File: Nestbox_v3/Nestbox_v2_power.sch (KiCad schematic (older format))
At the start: 27 parts, among them J201 BATT_CONN_01X02, Q201 Q_PMOS_DGS, U201 TPS62745, U202 LTC3534, U203 LP5907

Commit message: finished V3 pcb. ORDERED
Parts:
- removed JP201: VAA_Jumper_SELECT_Dual, Pin_Headers:Pin_Header_Straight_1x03, symbol Jumper_SELECT_Dual
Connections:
- net VAA: now also C204.1, U203.5 (VOUT)
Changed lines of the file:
@@
 L VAA #PWR013
 U 1 1 5B0757D1
-P 4700 5750
-F 0 "#PWR013" H 4700 5600 50  0001 C CNN
-F 1 "VAA" H 4717 5923 50  0000 C CNN
-F 2 "" H 4700 5750 50  0001 C CNN
-F 3 "" H 4700 5750 50  0001 C CNN
-	1    4700 5750
+P 4400 6050
+F 0 "#PWR013" H 4400 5900 50  0001 C CNN
+F 1 "VAA" H 4417 6223 50  0000 C CNN
+F 2 "" H 4400 6050 50  0001 C CNN
+F 3 "" H 4400 6050 50  0001 C CNN
+	1    4400 6050
 	1    0    0    -1
 $EndComp
@@
 	1950 6350 3100 6350
 Wire Wire Line
-	3100 6450 2900 6450
+	2900 6450 3100 6450
 Wire Wire Line
 	4100 6350 4400 6350
@@
 	2500 6850 2500 6750
 Wire Wire Line
-	2500 5550 2500 6450
+	2500 6350 2500 6450
 Connection ~ 2500 6350
 Wire Wire Line
@@
 	4400 6800 4400 6750
 $Comp
-L Jumper_SELECT_Dual JP201
-U 1 1 5B0C48C9
-P 4400 5800
-F 0 "JP201" H 4450 5700 50  0000 L CNN
-F 1 "VAA_Jumper_SELECT_Dual" H 4400 5900 50  0000 C BNN
-F 2 "Pin_Headers:Pin_Header_Straight_1x03" H 4400 5800 50  0001 C CNN
-F 3 "" H 4400 5800 50  0001 C CNN
-	1    4400 5800
-	0    -1   -1   0
-$EndComp
-Wire Wire Line
-	4700 5750 4700 5800
-Wire Wire Line
-	4700 5800 4500 5800
-Wire Wire Line
-	4400 5550 2500 5550
-$Comp
 L LTC3534 U202

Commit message: exchanged both inductor footprints.
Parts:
- L201: value 4.7uH -> 5uH; MFG_PN XFL3010-472MEB -> (none); MPN (none) -> MSS7341-502NLD
- L202: value 5uH -> 4.7uH; MFR_PN MSS7341-502NLD -> (none); MPN (none) -> XFL3010-472MEB
- Q201: value Q_PMOS_DGS -> TPH1R712MDL1Q; MPN (none) -> TPH1R712MDL1Q
- R201: value 100k -> 82k
- R202: value 50k -> 47k
- R204: value 162k -> 162k 1%
- R205: value 649k -> 649k 1%
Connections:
- net at C205.1, JP203.1, U201.5 (VOUT): now also L202.2; no longer L201.2
- net at L201.1: now also U202.5 (SW1); no longer U201.2 (SW)
- net at L202.1: now also U201.2 (SW); no longer U202.5 (SW1)
- net at U202.6 (SW2): now also L201.2; no longer L202.2
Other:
- moved on the sheet: L201, L202
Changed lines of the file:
@@
 L L L201
 U 1 1 5A021289
-P 4750 1500
-F 0 "L201" V 4940 1500 50  0000 C CNN
-F 1 "4.7uH" V 4849 1500 50  0000 C CNN
-F 2 "Inductors:Inductor_Taiyo-Yuden_NR-60xx_HandSoldering" H 4750 1500 50  0001 C CNN
-F 3 "" H 4750 1500 50  0001 C CNN
-F 4 "XFL3010-472MEB" V 4750 1500 60  0001 C CNN "MFG_PN"
-	1    4750 1500
+P 3700 3450
+F 0 "L201" V 3890 3450 50  0000 C CNN
+F 1 "5uH" V 3799 3450 50  0000 C CNN
+F 2 "Inductors:Inductor_Taiyo-Yuden_NR-60xx_HandSoldering" H 3700 3450 50  0001 C CNN
+F 3 "" H 3700 3450 50  0001 C CNN
+F 4 "MSS7341-502NLD" V 3700 3450 60  0001 C CNN "MPN"
+	1    3700 3450
 	0    -1   -1   0
 $EndComp
@@
 L L L202
 U 1 1 5A022A1C
-P 3700 3450
-F 0 "L202" V 3890 3450 50  0000 C CNN
-F 1 "5uH" V 3799 3450 50  0000 C CNN
-F 2 "Inductors:Inductor_Taiyo-Yuden_NR-30xx" H 3700 3450 50  0001 C CNN
-F 3 "" H 3700 3450 50  0001 C CNN
-F 4 "MSS7341-502NLD" V 3700 3450 60  0001 C CNN "MFR_PN"
-	1    3700 3450
+P 4750 1500
+F 0 "L202" V 4940 1500 50  0000 C CNN
+F 1 "4.7uH" V 4849 1500 50  0000 C CNN
+F 2 "Inductors:Inductor_Taiyo-Yuden_NR-30xx" H 4750 1500 50  0001 C CNN
+F 3 "" H 4750 1500 50  0001 C CNN
+F 4 "XFL3010-472MEB" V 4750 1500 60  0001 C CNN "MPN"
+	1    4750 1500
 	0    -1   -1   0
 $EndComp
@@
 P 5900 4300
 F 0 "R205" V 5693 4300 50  0000 C CNN
-F 1 "649k" V 5784 4300 50  0000 C CNN
+F 1 "649k 1%" V 5784 4300 50  0000 C CNN
 F 2 "Resistors_SMD:R_0603" V 5830 4300 50  0001 C CNN
 F 3 "" H 5900 4300 50  0001 C CNN
@@
 P 5650 4550
 F 0 "R204" H 5580 4504 50  0000 R CNN
-F 1 "162k" H 5580 4595 50  0000 R CNN
+F 1 "162k 1%" H 5580 4595 50  0000 R CNN
 F 2 "Resistors_SMD:R_0603" V 5580 4550 50  0001 C CNN
 F 3 "" H 5650 4550 50  0001 C CNN
@@
 P 2550 2350
 F 0 "R201" V 2343 2350 50  0000 C CNN
-F 1 "100k" V 2434 2350 50  0000 C CNN
+F 1 "82k" V 2434 2350 50  0000 C CNN
 F 2 "Resistors_SMD:R_0603" V 2480 2350 50  0001 C CNN
 F 3 "" H 2550 2350 50  0001 C CNN
@@
 P 2550 2800
 F 0 "R202" V 2343 2800 50  0000 C CNN
-F 1 "50k" V 2434 2800 50  0000 C CNN
+F 1 "47k" V 2434 2800 50  0000 C CNN
 F 2 "Resistors_SMD:R_0603" V 2480 2800 50  0001 C CNN
 F 3 "" H 2550 2800 50  0001 C CNN
@@
 P 9000 3150
 F 0 "Q201" H 9200 3200 50  0000 L CNN
-F 1 "Q_PMOS_DGS" H 9200 3100 50  0000 L CNN
+F 1 "TPH1R712MDL1Q" H 9200 3100 50  0000 L CNN
 F 2 "Octanis3:TDSON-8-1_HandSoldering" H 9200 3250 50  0001 C CNN
 F 3 "" H 9000 3150 50  0001 C CNN
+F 4 "TPH1R712MDL1Q" H 9000 3150 60  0001 C CNN "MPN"
 	1    9000 3150
 	0    1    1    0

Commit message: added MPN for all components for PCBA
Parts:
- C201, C203, C205, C206, C207: MPN (none) -> CC0805KKX5R8BB106
- C202, C204: MPN (none) -> CC0603KRX7R8BB105
- C208: MPN (none) -> CC0603JRNPO9BN331
- C209: MPN (none) -> CC0603JRNPO9BN100
- C210: MPN (none) -> CC0603JRNPO9BN330
- Q201: MouserLink (none) -> https://www.mouser.ch/ProductDetail/Toshiba/TPH1R712MDL1Q?q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
- R201, R207, R208: MPN (none) -> RC0603FR-0782KL
- R202: MPN (none) -> RC0603FR-0747KL
- R203: MPN (none) -> RC0603JR-0710KL
- R204: MPN (none) -> RC0603FR-07162KL
- R205: MPN (none) -> RC0603FR-07649KL
- R206: MPN (none) -> RC0603JR-0715KL
- U201: MPN (none) -> TPS62745DSSR
- U202: MPN (none) -> LTC3534EDHC#PBF
- U203: MPN (none) -> LP5907MFX-3.0/NOPB
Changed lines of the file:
@@
-EESchema Schematic File Version 2
+EESchema Schematic File Version 4
 LIBS:power
 LIBS:device
@@
 LIBS:contrib
 LIBS:valves
-LIBS:Octanis3
 LIBS:Nestbox_v2-cache
-EELAYER 25 0
+EELAYER 26 0
 EELAYER END
 $Descr A4 11693 8268
@@
 F 2 "Capacitors_SMD:C_0805" H 1788 2000 50  0001 C CNN
 F 3 "" H 1750 2150 50  0001 C CNN
+F 4 "CC0805KKX5R8BB106" H 0   0   50  0001 C CNN "MPN"
 	1    1750 2150
 	1    0    0    -1
@@
 F 2 "Capacitors_SMD:C_0805" H 2188 4250 50  0001 C CNN
 F 3 "" H 2150 4400 50  0001 C CNN
+F 4 "CC0805KKX5R8BB106" H 0   0   50  0001 C CNN "MPN"
 	1    2150 4400
 	1    0    0    -1
@@
 F 2 "Resistors_SMD:R_0603" V 5830 4300 50  0001 C CNN
 F 3 "" H 5900 4300 50  0001 C CNN
+F 4 "RC0603FR-07649KL" H 0   0   50  0001 C CNN "MPN"
 	1    5900 4300
 	0    1    1    0
@@
 F 2 "Resistors_SMD:R_0603" V 5580 4550 50  0001 C CNN
 F 3 "" H 5650 4550 50  0001 C CNN
+F 4 "RC0603FR-07162KL" H 0   0   50  0001 C CNN "MPN"
 	1    5650 4550
 	-1   0    0    1
@@
 F 2 "Capacitors_SMD:C_0805" H 6338 4250 50  0001 C CNN
 F 3 "" H 6300 4400 50  0001 C CNN
+F 4 "CC0805KKX5R8BB106" H 0   0   50  0001 C CNN "MPN"
 	1    6300 4400
 	1    0    0    -1
@@
 F 2 "Capacitors_SMD:C_0805" H 6738 4250 50  0001 C CNN
 F 3 "" H 6700 4400 50  0001 C CNN
+F 4 "CC0805KKX5R8BB106" H 0   0   50  0001 C CNN "MPN"
 	1    6700 4400
 	1    0    0    -1
@@
 F 2 "Capacitors_SMD:C_0805" H 5338 2000 50  0001 C CNN
 F 3 "" H 5300 2150 50  0001 C CNN
+F 4 "CC0805KKX5R8BB106" H 0   0   50  0001 C CNN "MPN"
 	1    5300 2150
 	1    0    0    -1
@@
 F 2 "texasinstruments:SOT23-5" H 3500 6150 50  0001 C CNN
 F 3 "" H 3600 6400 50  0001 C CNN
+F 4 "LP5907MFX-3.0/NOPB" H 0   0   50  0001 C CNN "MPN"
 	1    3600 6400
 	1    0    0    -1
@@
 F 2 "Octanis3:WSON_3x2mm_12pin" H 3250 1450 60  0001 C CNN
 F 3 "" H 3250 1450 60  0001 C CNN
+F 4 "TPS62745DSSR" H 0   0   50  0001 C CNN "MPN"
 	1    3250 1450
 	1    0    0    -1
@@
 F 2 "Resistors_SMD:R_0603" V 2480 2350 50  0001 C CNN
 F 3 "" H 2550 2350 50  0001 C CNN
+F 4 "RC0603FR-0782KL" H 0   0   50  0001 C CNN "MPN"
 	1    2550 2350
 	-1   0    0    1
@@
 F 2 "Resistors_SMD:R_0603" V 2480 2800 50  0001 C CNN
 F 3 "" H 2550 2800 50  0001 C CNN
+F 4 "RC0603FR-0747KL" H 0   0   50  0001 C CNN "MPN"
 	1    2550 2800
 	-1   0    0    1
@@
 F 2 "Capacitors_SMD:C_0603" H 2538 6450 50  0001 C CNN
 F 3 "" H 2500 6600 50  0001 C CNN
+F 4 "CC0603KRX7R8BB105" H 0   0   50  0001 C CNN "MPN"
 	1    2500 6600
 	1    0    0    -1
@@
 F 2 "Capacitors_SMD:C_0603" H 4438 6450 50  0001 C CNN
 F 3 "" H 4400 6600 50  0001 C CNN
+F 4 "CC0603KRX7R8BB105" H 0   0   50  0001 C CNN "MPN"
 	1    4400 6600
 	1    0    0    -1
@@
 F 2 "SeeedOPL-IC-2016:SSOP16-0.635-5X4MM" H 3250 3700 60  0001 C CNN
 F 3 "" H 3250 3700 60  0001 C CNN
+F 4 "LTC3534EDHC#PBF" H 0   0   50  0001 C CNN "MPN"
 	1    3250 3700
 	1    0    0    -1
@@
 F 2 "Resistors_SMD:R_0603" V 4680 4050 50  0001 C CNN
 F 3 "" H 4750 4050 50  0001 C CNN
+F 4 "RC0603JR-0710KL" H 0   0   50  0001 C CNN "MPN"
 	1    4750 4050
 	0    1    1    0
@@
 F 2 "Capacitors_SMD:C_0603" H 5188 3900 50  0001 C CNN
 F 3 "" H 5150 4050 50  0001 C CNN
+F 4 "CC0603JRNPO9BN330" H 0   0   50  0001 C CNN "MPN"
 	1    5150 4050
 	0    -1   -1   0
@@
 F 2 "Resistors_SMD:R_0603" V 5080 4450 50  0001 C CNN
 F 3 "" H 5150 4450 50  0001 C CNN
+F 4 "RC0603JR-0715KL" H 0   0   50  0001 C CNN "MPN"
 	1    5150 4450
 	0    -1   -1   0
@@
 F 2 "Capacitors_SMD:C_0603" H 4788 4300 50  0001 C CNN
 F 3 "" H 4750 4450 50  0001 C CNN
+F 4 "CC0603JRNPO9BN331" H 0   0   50  0001 C CNN "MPN"
 	1    4750 4450
 	0    1    1    0
@@
 F 2 "Capacitors_SMD:C_0603" H 5038 4600 50  0001 C CNN
 F 3 "" H 5000 4750 50  0001 C CNN
+F 4 "CC0603JRNPO9BN100" H 0   0   50  0001 C CNN "MPN"
 	1    5000 4750
 	0    1    1    0
@@
 F 3 "" H 9000 3150 50  0001 C CNN
 F 4 "TPH1R712MDL1Q" H 9000 3150 60  0001 C CNN "MPN"
+F 5 "https://www.mouser.ch/ProductDetail/Toshiba/TPH1R712MDL1Q?qs=sGAEpiMZZMvNM%2fd3q5fCV4Bsm%252b4NPS2VEWd3q01qzE4%3d" H 0   0   50  0001 C CNN "MouserLink"
 	1    9000 3150
 	0    1    1    0
@@
 F 2 "Resistors_SMD:R_0603" V 1630 4150 50  0001 C CNN
 F 3 "" H 1700 4150 50  0001 C CNN
+F 4 "RC0603FR-0782KL" H 0   0   50  0001 C CNN "MPN"
 	1    1700 4150
 	-1   0    0    1
@@
 F 2 "Resistors_SMD:R_0603" V 2930 6650 50  0001 C CNN
 F 3 "" H 3000 6650 50  0001 C CNN
+F 4 "RC0603FR-0782KL" H 0   0   50  0001 C CNN "MPN"
 	1    3000 6650
 	-1   0    0    1

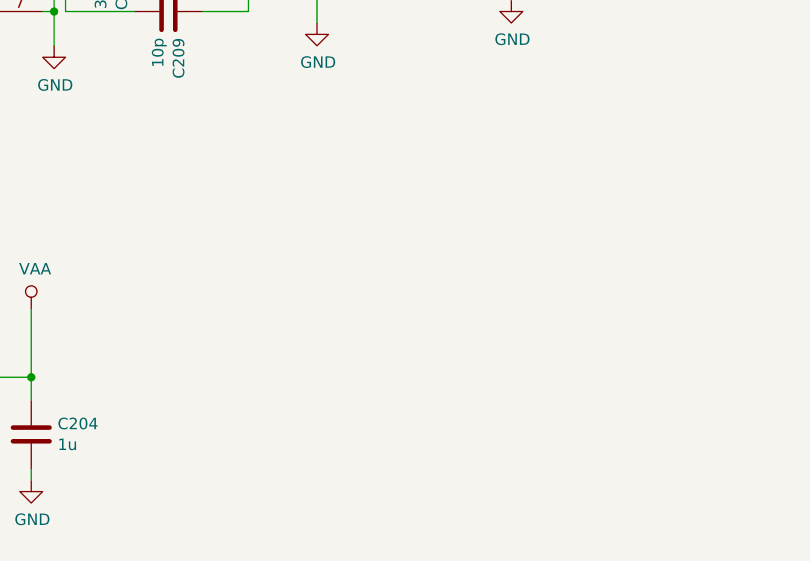
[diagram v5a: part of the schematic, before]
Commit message: production status nestbox v3
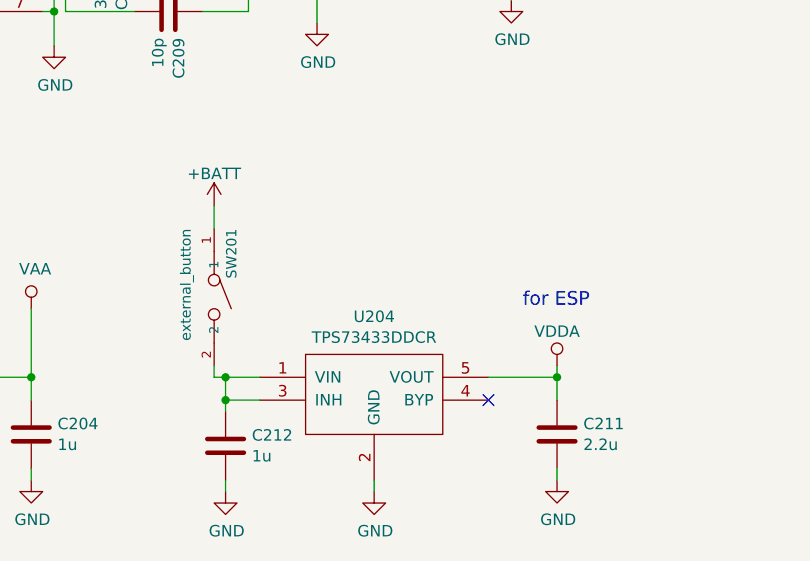
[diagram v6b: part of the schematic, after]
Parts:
- added C211: 2.2u, Capacitors_SMD:C_0603, symbol C
- added C212: 1u, Capacitors_SMD:C_0603, symbol C
- added SW201: external_button, Buttons_Switches_SMD:SW_SPST_B3U-1000P, symbol SMD-BUTTON_2P-3.0X2.5X1.2+0.4MM_
- added U204: TPS73433DDCR, texasinstruments:SOT23-5, symbol LD3985M
- JP203: footprint Pin_Headers:Pin_Header_Straight_1x02 -> Connect:GS2
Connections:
- net +BATT: now also SW201.1
- net GND: now also C211.2, C212.2, U204.2 (GND)
- new net: C212.1, SW201.2, U204.1 (VIN), U204.3 (INH)
- new net VDDA: C211.1, U204.5 (VOUT)
- no-connect marks 2 -> 3
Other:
- note added: "for ESP\n"
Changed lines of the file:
@@
 F 0 "JP203" H 6450 2164 50  0000 C CNN
 F 1 "Jumper_3V3" H 6450 2073 50  0000 C CNN
-F 2 "Pin_Headers:Pin_Header_Straight_1x02" H 6450 1900 50  0001 C CNN
+F 2 "Connect:GS2" H 6450 1900 50  0001 C CNN
 F 3 "" H 6450 1900 50  0001 C CNN
 	1    6450 1900
@@
 	1    0    0    -1
 $EndComp
+$Comp
+L LD3985M U204
+U 1 1 5BF55BCD
+P 5900 6400
+F 0 "U204" H 5900 6715 50  0000 C CNN
+F 1 "TPS73433DDCR" H 5900 6624 50  0000 C CNN
+F 2 "texasinstruments:SOT23-5" H 5800 6150 50  0001 C CNN
+F 3 "" H 5900 6400 50  0001 C CNN
+F 4 "LP5907MFX-3.0/NOPB" H 2300 0   50  0001 C CNN "MPN"
+	1    5900 6400
+	1    0    0    -1
+$EndComp
+$Comp
+L C C211
+U 1 1 5BF55EF1
+P 6700 6600
+F 0 "C211" H 6815 6646 50  0000 L CNN
+F 1 "2.2u" H 6815 6555 50  0000 L CNN
+F 2 "Capacitors_SMD:C_0603" H 6738 6450 50  0001 C CNN
+F 3 "" H 6700 6600 50  0001 C CNN
+F 4 "CC0603KRX7R8BB105" H 2300 0   50  0001 C CNN "MPN"
+	1    6700 6600
+	1    0    0    -1
+$EndComp
+Wire Wire Line
+	6400 6350 6700 6350
+Wire Wire Line
+	6700 6300 6700 6450
+$Comp
+L GND #PWR025
+U 1 1 5BF56057
+P 6700 6800
+F 0 "#PWR025" H 6700 6550 50  0001 C CNN
+F 1 "GND" H 6705 6627 50  0000 C CNN
+F 2 "" H 6700 6800 50  0001 C CNN
+F 3 "" H 6700 6800 50  0001 C CNN
+	1    6700 6800
+	1    0    0    -1
+$EndComp
+Wire Wire Line
+	6700 6750 6700 6800
+$Comp
+L +BATT #PWR026
+U 1 1 5BF5619D
+P 5200 5600
+F 0 "#PWR026" H 5200 5450 50  0001 C CNN
+F 1 "+BATT" H 5200 5740 50  0000 C CNN
+F 2 "" H 5200 5600 50  0001 C CNN
+F 3 "" H 5200 5600 50  0001 C CNN
+	1    5200 5600
+	1    0    0    -1
+$EndComp
+Wire Wire Line
+	5200 6300 5200 6350
+Wire Wire Line
+	5200 6350 5400 6350
+Wire Wire Line
+	5250 6450 5400 6450
+$Comp
+L GND #PWR027
+U 1 1 5BF56425
+P 5900 6850
+F 0 "#PWR027" H 5900 6600 50  0001 C CNN
+F 1 "GND" H 5905 6677 50  0000 C CNN
+F 2 "" H 5900 6850 50  0001 C CNN
+F 3 "" H 5900 6850 50  0001 C CNN
+	1    5900 6850
+	1    0    0    -1
+$EndComp
+Wire Wire Line
+	5900 6850 5900 6800
+NoConn ~ 6400 6450
+$Comp
+L VDDA #PWR028
+U 1 1 5BF5678A
+P 6700 6300
+F 0 "#PWR028" H 6700 6150 50  0001 C CNN
+F 1 "VDDA" H 6700 6450 50  0000 C CNN
+F 2 "" H 6700 6300 50  0001 C CNN
+F 3 "" H 6700 6300 50  0001 C CNN
+	1    6700 6300
+	1    0    0    -1
+$EndComp
+Connection ~ 6700 6350
+Text Notes 6550 6050 0    60   ~ 0
+for ESP\n
+$Comp
+L SMD-BUTTON_2P-3.0X2.5X1.2+0.4MM_ SW201
+U 1 1 5BF57033
+P 5200 6000
+F 0 "SW201" H 4900 6050 45  0000 L BNN
+F 1 "external_button" H 4900 5850 45  0000 L BNN
+F 2 "Buttons_Switches_SMD:SW_SPST_B3U-1000P" H 5200 6000 60  0001 C CNN
+F 3 "" H 5200 6000 60  0001 C CNN
+F 4 "B3U-1000P-2P-SMD" H 5230 6150 20  0001 C CNN "MPN"
+F 5 "311020047" H 5230 6150 20  0001 C CNN "SKU"
+	1    5200 6000
+	0    1    1    0
+$EndComp
+Wire Wire Line
+	5200 5600 5200 5700
+Wire Wire Line
+	5250 6350 5250 6500
+Connection ~ 5250 6350
+$Comp
+L C C212
+U 1 1 5BF590BB
+P 5250 6650
+F 0 "C212" H 5365 6696 50  0000 L CNN
+F 1 "1u" H 5365 6605 50  0000 L CNN
+F 2 "Capacitors_SMD:C_0603" H 5288 6500 50  0001 C CNN
+F 3 "" H 5250 6650 50  0001 C CNN
+F 4 "CC0603KRX7R8BB105" H 850 50  50  0001 C CNN "MPN"
+	1    5250 6650
+	1    0    0    -1
+$EndComp
+Connection ~ 5250 6450
+$Comp
+L GND #PWR029
+U 1 1 5BF591CD
+P 5250 6850
+F 0 "#PWR029" H 5250 6600 50  0001 C CNN
+F 1 "GND" H 5255 6677 50  0000 C CNN
+F 2 "" H 5250 6850 50  0001 C CNN
+F 3 "" H 5250 6850 50  0001 C CNN
+	1    5250 6850
+	1    0    0    -1
+$EndComp
+Wire Wire Line
+	5250 6850 5250 6800
 $EndSCHEMATC
